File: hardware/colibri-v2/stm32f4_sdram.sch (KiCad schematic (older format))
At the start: 8 parts, among them U3 IS42S16400J

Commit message: Replaced the SDRAM with TFBGA-54
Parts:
- removed U3: IS42S16400J, symbol IS42S16400J
- added U3: IS42S16400J-7BLI, symbol IS42S16400J-7BLI
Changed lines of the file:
@@
 Comment4 ""
 $EndDescr
-$Comp
-L IS42S16400J U3
-U 1 1 55895059
-P 5000 2900
-F 0 "U3" H 5450 4550 60  0000 C CNN
-F 1 "IS42S16400J" H 4800 4550 60  0000 C CNN
-F 2 "" H 5000 3400 60  0001 C CNN
-F 3 "" H 5000 3400 60  0000 C CNN
-	1    5000 2900
-	1    0    0    -1
-$EndComp
 Text Label 3500 1400 0    60   ~ 0
 FMC_A0
@@
 Text Label 3200 2500 2    60   ~ 0
 FMC_A[0..11]
+$Comp
+L IS42S16400J-7BLI U3
+U 1 1 56CC32E5
+P 5000 2900
+F 0 "U3" H 5450 4550 60  0000 C CNN
+F 1 "IS42S16400J-7BLI" H 4800 4550 60  0000 C CNN
+F 2 "" H 5000 3400 60  0000 C CNN
+F 3 "" H 5000 3400 60  0000 C CNN
+	1    5000 2900
+	1    0    0    -1
+$EndComp
 $EndSCHEMATC

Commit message: Assigning footprints
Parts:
- U3: footprint (none) -> Sigmadrone:tfbga-54
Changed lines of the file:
@@
 F 0 "U3" H 5450 4550 60  0000 C CNN
 F 1 "IS42S16400J-7BLI" H 4800 4550 60  0000 C CNN
-F 2 "" H 5000 3400 60  0000 C CNN
+F 2 "Sigmadrone:tfbga-54" H 5000 3400 60  0001 C CNN
 F 3 "" H 5000 3400 60  0000 C CNN
 	1    5000 2900

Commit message: Changed the tfbga footprints to use smaller pads
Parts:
- U3: footprint Sigmadrone:tfbga-54 -> Sigmadrone:tfbga-54-35
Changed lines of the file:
@@
 F 0 "U3" H 5450 4550 60  0000 C CNN
 F 1 "IS42S16400J-7BLI" H 4800 4550 60  0000 C CNN
-F 2 "Sigmadrone:tfbga-54" H 5000 3400 60  0001 C CNN
+F 2 "Sigmadrone:tfbga-54-35" H 5000 3400 60  0001 C CNN
 F 3 "" H 5000 3400 60  0000 C CNN
 	1    5000 2900

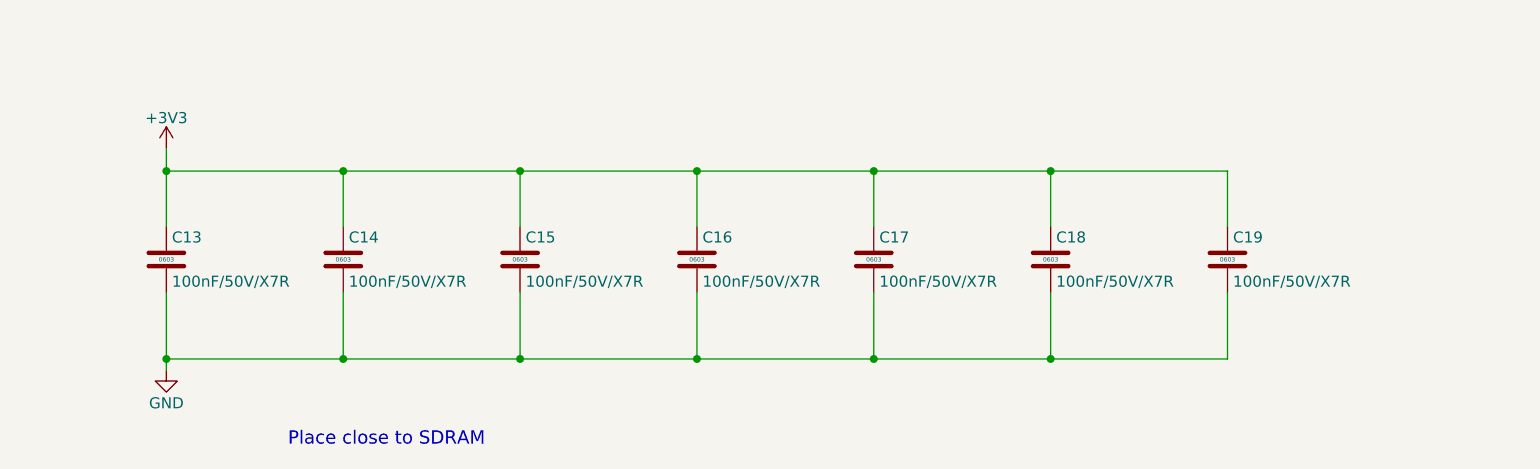
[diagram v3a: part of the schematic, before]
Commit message: Changed the footprints of SDRAM filter capacitors
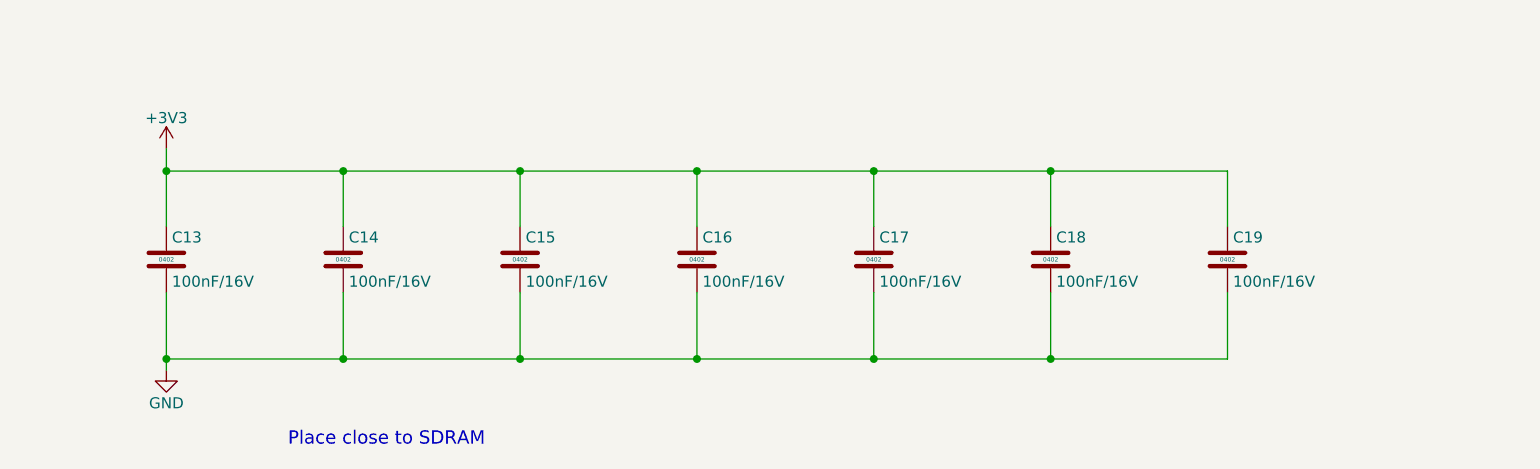
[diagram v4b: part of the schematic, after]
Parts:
- C13, C14, C15, C16, C17, C18, C19: value 100nF/50V/X7R -> 100nF/16V; footprint Capacitors_SMD:C_0603 -> Capacitors_SMD:C_0402; Part 1414028 -> 1288252; SMT 0603 -> 0402
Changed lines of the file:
@@
 P 7200 5750
 F 0 "C19" H 7225 5850 50  0000 L CNN
-F 1 "100nF/50V/X7R" H 7225 5650 50  0000 L CNN
-F 2 "Capacitors_SMD:C_0603" H 7230 5600 30  0001 L CNN
+F 1 "100nF/16V" H 7225 5650 50  0000 L CNN
+F 2 "Capacitors_SMD:C_0402" H 7230 5600 30  0001 L CNN
 F 3 "" H 7225 5850 60  0000 L CNN
-F 4 "0603" H 7200 5750 20  0000 C CNN "SMT"
-F 5 "1414028" H 7230 5560 30  0001 L CNN "Part"
+F 4 "0402" H 7200 5750 20  0000 C CNN "SMT"
+F 5 "1288252" H 7230 5560 30  0001 L CNN "Part"
 F 6 "Farnell" H 7230 5520 30  0001 L CNN "Provider"
 	1    7200 5750
@@
 P 6400 5750
 F 0 "C18" H 6425 5850 50  0000 L CNN
-F 1 "100nF/50V/X7R" H 6425 5650 50  0000 L CNN
-F 2 "Capacitors_SMD:C_0603" H 6430 5600 30  0001 L CNN
+F 1 "100nF/16V" H 6425 5650 50  0000 L CNN
+F 2 "Capacitors_SMD:C_0402" H 6430 5600 30  0001 L CNN
 F 3 "" H 6425 5850 60  0000 L CNN
-F 4 "0603" H 6400 5750 20  0000 C CNN "SMT"
-F 5 "1414028" H 6430 5560 30  0001 L CNN "Part"
+F 4 "0402" H 6400 5750 20  0000 C CNN "SMT"
+F 5 "1288252" H 6430 5560 30  0001 L CNN "Part"
 F 6 "Farnell" H 6430 5520 30  0001 L CNN "Provider"
 	1    6400 5750
@@
 P 5600 5750
 F 0 "C17" H 5625 5850 50  0000 L CNN
-F 1 "100nF/50V/X7R" H 5625 5650 50  0000 L CNN
-F 2 "Capacitors_SMD:C_0603" H 5630 5600 30  0001 L CNN
+F 1 "100nF/16V" H 5625 5650 50  0000 L CNN
+F 2 "Capacitors_SMD:C_0402" H 5630 5600 30  0001 L CNN
 F 3 "" H 5625 5850 60  0000 L CNN
-F 4 "0603" H 5600 5750 20  0000 C CNN "SMT"
-F 5 "1414028" H 5630 5560 30  0001 L CNN "Part"
+F 4 "0402" H 5600 5750 20  0000 C CNN "SMT"
+F 5 "1288252" H 5630 5560 30  0001 L CNN "Part"
 F 6 "Farnell" H 5630 5520 30  0001 L CNN "Provider"
 	1    5600 5750
@@
 P 4800 5750
 F 0 "C16" H 4825 5850 50  0000 L CNN
-F 1 "100nF/50V/X7R" H 4825 5650 50  0000 L CNN
-F 2 "Capacitors_SMD:C_0603" H 4830 5600 30  0001 L CNN
+F 1 "100nF/16V" H 4825 5650 50  0000 L CNN
+F 2 "Capacitors_SMD:C_0402" H 4830 5600 30  0001 L CNN
 F 3 "" H 4825 5850 60  0000 L CNN
-F 4 "0603" H 4800 5750 20  0000 C CNN "SMT"
-F 5 "1414028" H 4830 5560 30  0001 L CNN "Part"
+F 4 "0402" H 4800 5750 20  0000 C CNN "SMT"
+F 5 "1288252" H 4830 5560 30  0001 L CNN "Part"
 F 6 "Farnell" H 4830 5520 30  0001 L CNN "Provider"
 	1    4800 5750
@@
 P 4000 5750
 F 0 "C15" H 4025 5850 50  0000 L CNN
-F 1 "100nF/50V/X7R" H 4025 5650 50  0000 L CNN
-F 2 "Capacitors_SMD:C_0603" H 4030 5600 30  0001 L CNN
+F 1 "100nF/16V" H 4025 5650 50  0000 L CNN
+F 2 "Capacitors_SMD:C_0402" H 4030 5600 30  0001 L CNN
 F 3 "" H 4025 5850 60  0000 L CNN
-F 4 "0603" H 4000 5750 20  0000 C CNN "SMT"
-F 5 "1414028" H 4030 5560 30  0001 L CNN "Part"
+F 4 "0402" H 4000 5750 20  0000 C CNN "SMT"
+F 5 "1288252" H 4030 5560 30  0001 L CNN "Part"
 F 6 "Farnell" H 4030 5520 30  0001 L CNN "Provider"
 	1    4000 5750
@@
 P 3200 5750
 F 0 "C14" H 3225 5850 50  0000 L CNN
-F 1 "100nF/50V/X7R" H 3225 5650 50  0000 L CNN
-F 2 "Capacitors_SMD:C_0603" H 3230 5600 30  0001 L CNN
+F 1 "100nF/16V" H 3225 5650 50  0000 L CNN
+F 2 "Capacitors_SMD:C_0402" H 3230 5600 30  0001 L CNN
 F 3 "" H 3225 5850 60  0000 L CNN
-F 4 "0603" H 3200 5750 20  0000 C CNN "SMT"
-F 5 "1414028" H 3230 5560 30  0001 L CNN "Part"
+F 4 "0402" H 3200 5750 20  0000 C CNN "SMT"
+F 5 "1288252" H 3230 5560 30  0001 L CNN "Part"
 F 6 "Farnell" H 3230 5520 30  0001 L CNN "Provider"
 	1    3200 5750
@@
 P 2400 5750
 F 0 "C13" H 2425 5850 50  0000 L CNN
-F 1 "100nF/50V/X7R" H 2425 5650 50  0000 L CNN
-F 2 "Capacitors_SMD:C_0603" H 2430 5600 30  0001 L CNN
+F 1 "100nF/16V" H 2425 5650 50  0000 L CNN
+F 2 "Capacitors_SMD:C_0402" H 2430 5600 30  0001 L CNN
 F 3 "" H 2425 5850 60  0000 L CNN
-F 4 "0603" H 2400 5750 20  0000 C CNN "SMT"
-F 5 "1414028" H 2430 5560 30  0001 L CNN "Part"
+F 4 "0402" H 2400 5750 20  0000 C CNN "SMT"
+F 5 "1288252" H 2430 5560 30  0001 L CNN "Part"
 F 6 "Farnell" H 2430 5520 30  0001 L CNN "Provider"
 	1    2400 5750
